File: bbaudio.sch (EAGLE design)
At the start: 38 parts, among them IC1 TLV320AIC3106, J1 AUDIO-JACKERTHENVAR, J2 AUDIO-JACKERTHENVAR, J3 AUDIO-JACKERTHENVAR, J4 AUDIO-JACKERTHENVAR, U2 V_REG_MIC2920, U3 LMZ14203, U4 VREG

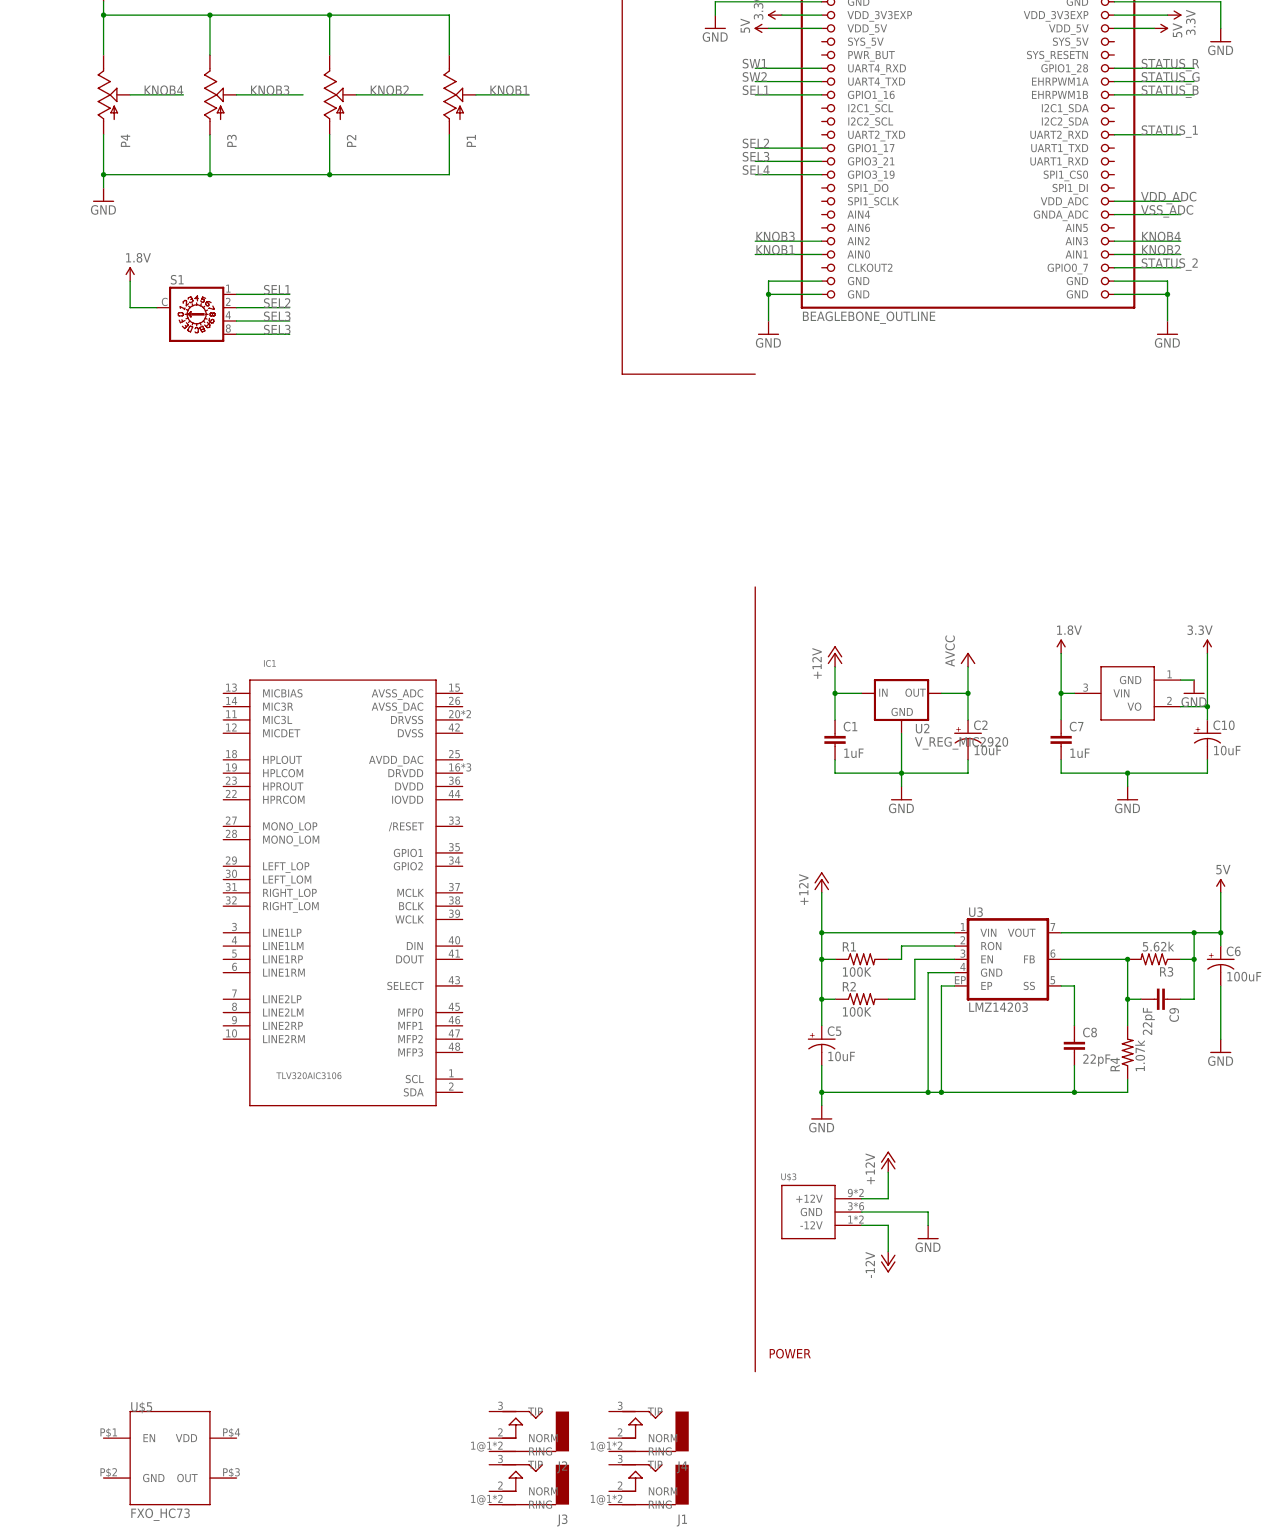
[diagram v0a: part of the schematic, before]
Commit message: Started wiring up the codec
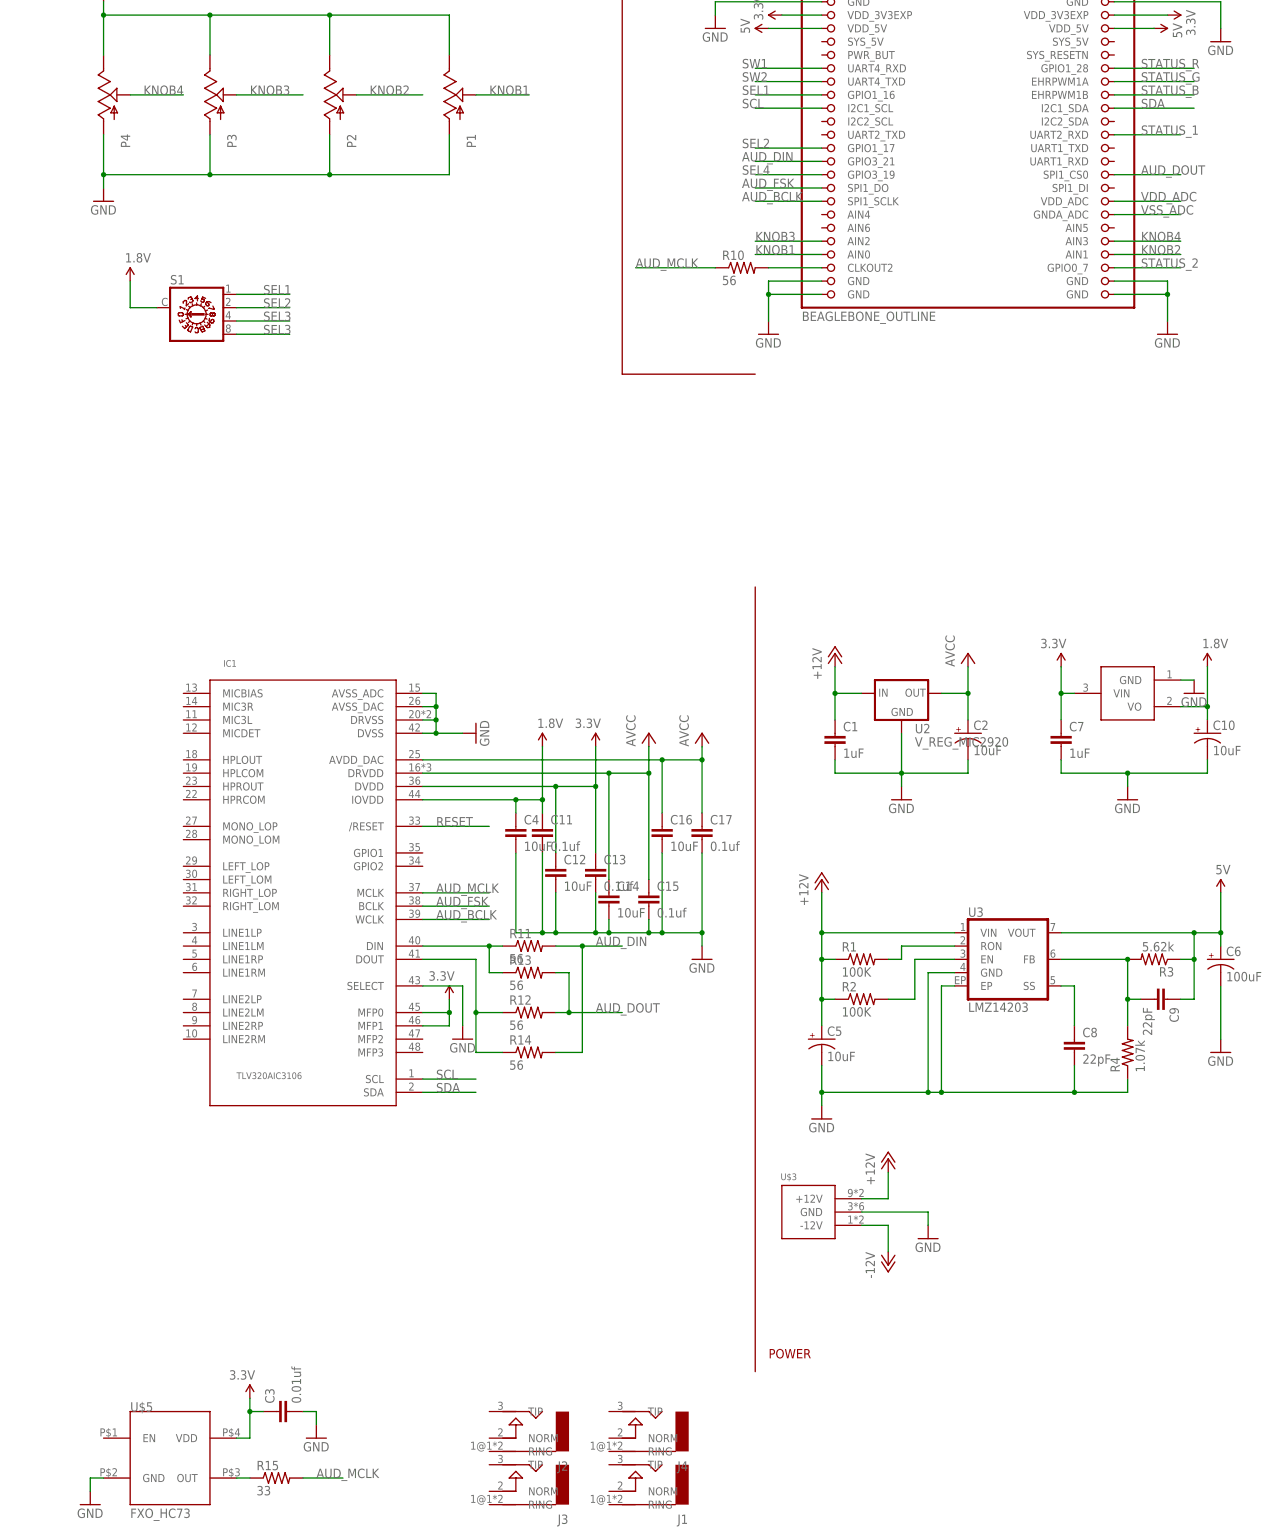
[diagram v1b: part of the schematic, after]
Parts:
- added C11, C13, C15, C17: 0.1uf, rcl:C-EUC0603
- added C12, C14, C16, C4: 10uF, rcl:C-EUC0603
- added C3: 0.01uf, rcl:C-EUC0603
- added R10, R11, R12, R13, R14: 56, SparkFun-Passives:RESISTOR0603-RES
- added R15: 33, SparkFun-Passives:RESISTOR0603-RES
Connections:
- new net AUD_BCLK: IC1.WCLK, U$1.SPI1_SCLK
- new net AUD_DIN: R11.2, R14.2, U$1.GPIO3_21
- new net AUD_DOUT: R12.2, R13.2, U$1.SPI1_CS0
- new net AUD_FSK: IC1.BCLK, U$1.SPI1_DO
- new net AUD_MCLK: IC1.MCLK, R10.1, R15.2
- new net N$10: IC1.DIN, R11.1, R13.1
- new net N$11: IC1.DOUT, R12.1, R14.1
- new net N$12: R15.1, U$5.OUT
- new net N$9: R10.2, U$1.CLKOUT2
- new net RESET: IC1./RESET
- new net SCL: IC1.SCL, U$1.I2C1_SCL
- new net SDA: IC1.SDA, U$1.I2C1_SDA
- net 1.8V: now also C10.+, C11.1, C4.1, IC1.IOVDD, U4.VO; no longer C7.1, U4.VIN
- net 3.3V: now also C12.1, C13.1, C3.1, C7.1, IC1.DVDD, IC1.MFP0, IC1.MFP1, U$5.VDD, U4.VIN; no longer C10.+, U4.VO
- net GND: now also C11.2, C12.2, C13.2, C14.2, C15.2, C16.2, C17.2, C3.2, C4.2, IC1.AVSS_ADC, IC1.AVSS_DAC, IC1.DRVSS, IC1.DVSS, IC1.SELECT, U$5.GND
- net SEL3: no longer U$1.GPIO3_21
- net VCC: now also C14.1, C15.1, C16.1, C17.1, IC1.AVDD_DAC, IC1.DRVDD
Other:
- moved on the sheet: IC1

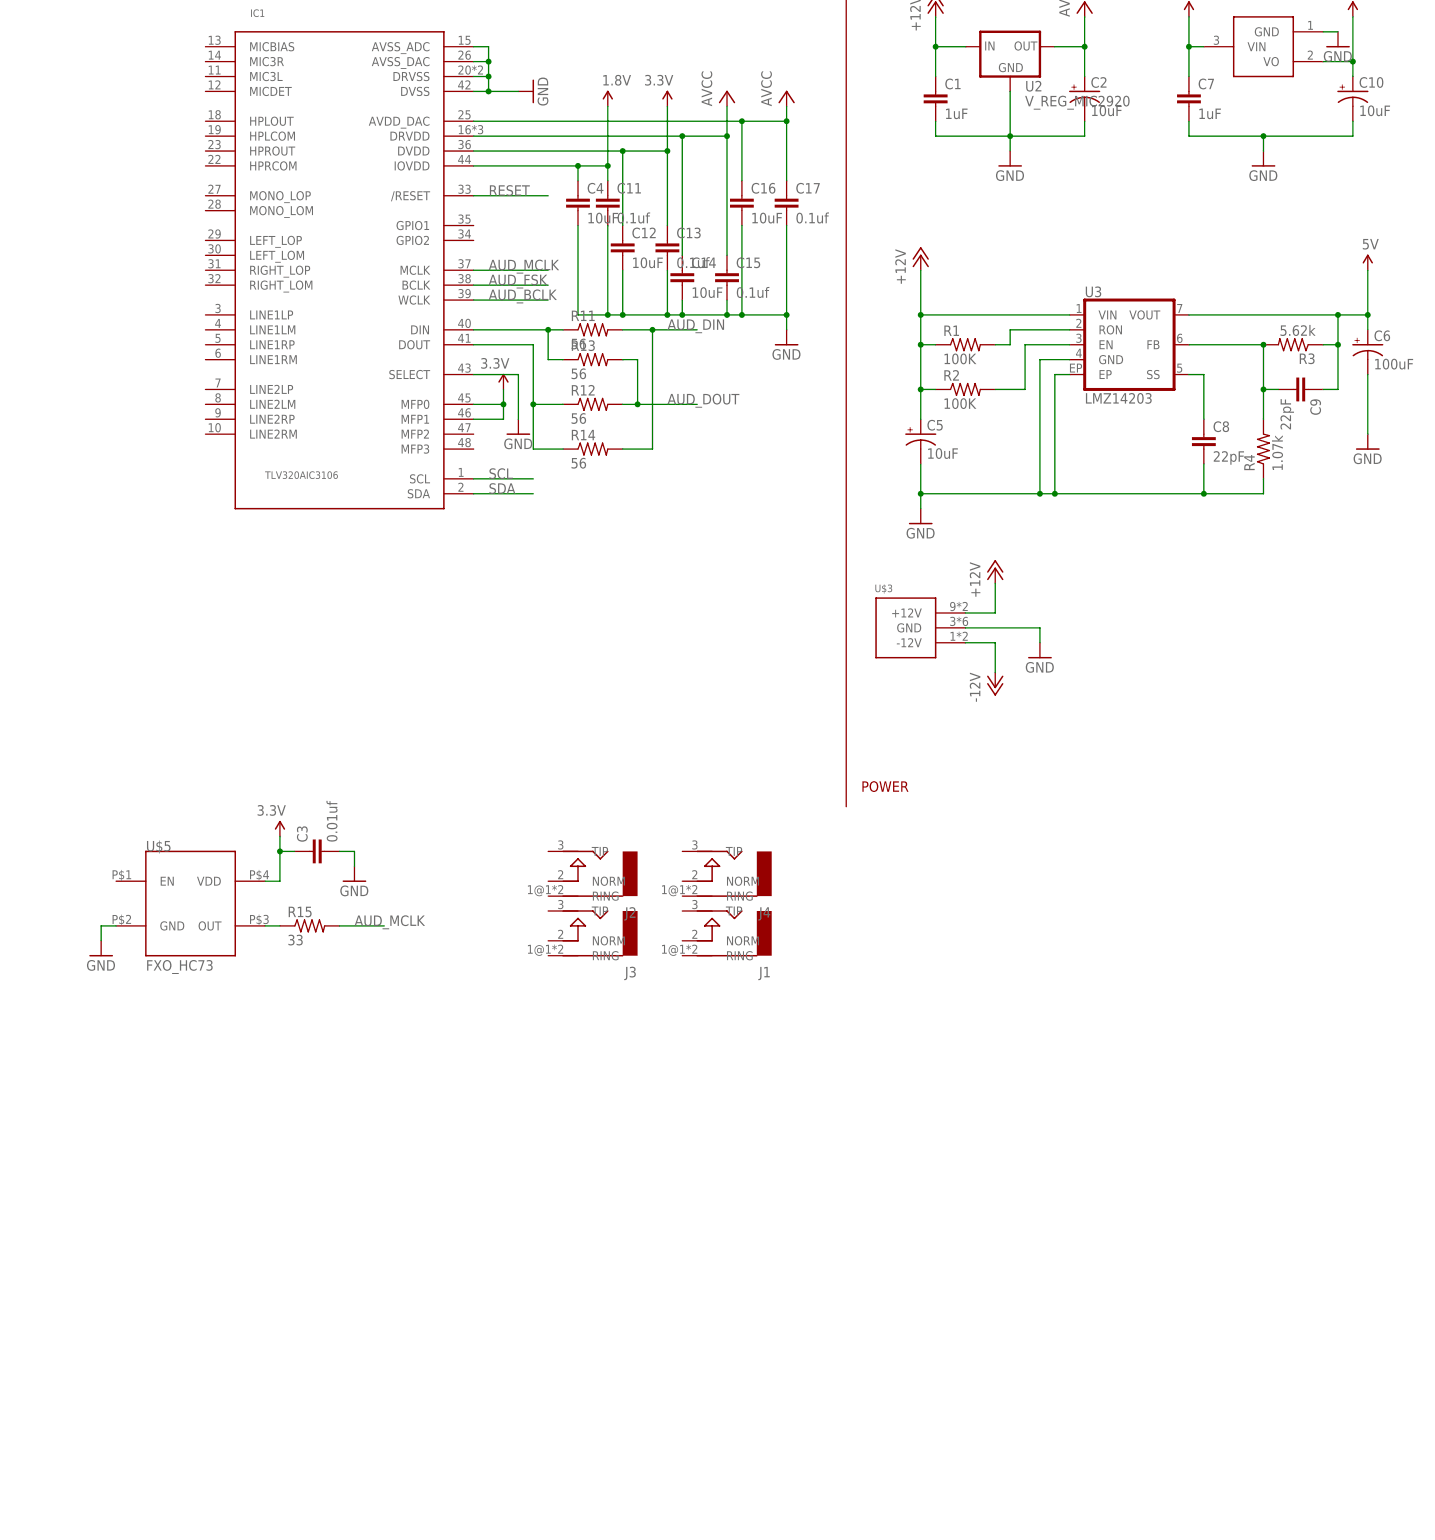
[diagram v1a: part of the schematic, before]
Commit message: Added audio i/o
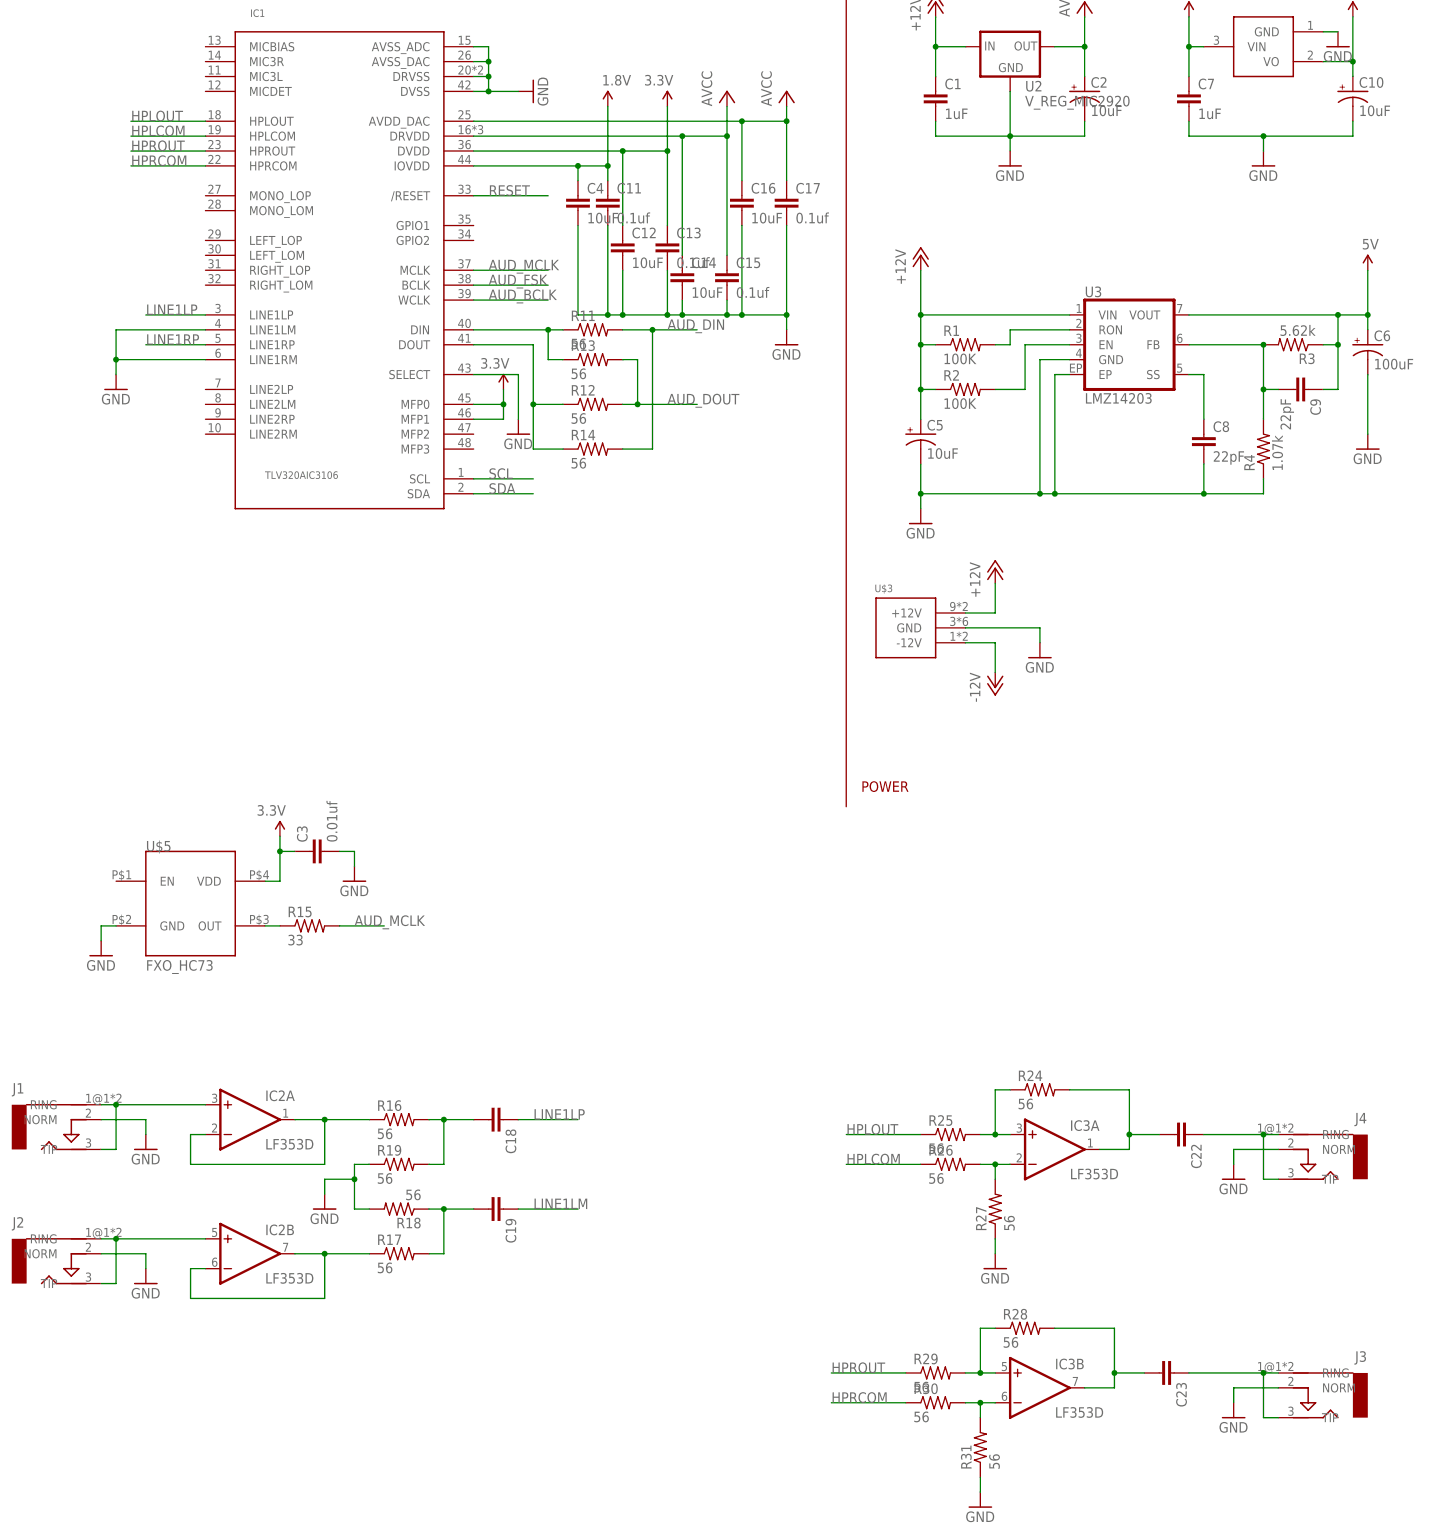
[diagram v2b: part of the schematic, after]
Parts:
- added C18, C19, C22, C23: (no value), SparkFun-Passives:CAP0805
- added IC2, IC3: LF353D, linear:LF353D
- added R16, R17, R18, R19, R24, R25, R26, R27, R28, R29, R30, R31: 56, SparkFun-Passives:RESISTOR0603-RES
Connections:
- new net HPLCOM: IC1.HPLCOM, R26.1
- new net HPLOUT: IC1.HPLOUT, R25.1
- new net HPRCOM: IC1.HPRCOM, R30.1
- new net HPROUT: IC1.HPROUT, R29.1
- new net LINE1LM: C19.1
- new net LINE1LP: C18.1, IC1.LINE1LP
- new net LINE1RP: IC1.LINE1RP
- new net N$14: IC2A.-IN, IC2A.OUT, R16.1
- new net N$15: C18.2, R16.2, R19.2
- new net N$16: IC2B.-IN, IC2B.OUT, R17.1
- new net N$17: C19.2, R17.2, R18.1
- new net N$18: IC2A.+IN, J1.RING, J1.TIP
- new net N$19: IC2B.+IN, J2.RING, J2.TIP
- new net N$20: C22.1, J4.RING, J4.TIP
- new net N$27: C22.2, IC3A.OUT, R24.2
- new net N$28: IC3A.+IN, R24.1, R25.2
- new net N$29: IC3A.-IN, R26.2, R27.2
- new net N$31: C23.2, IC3B.OUT, R28.2
- new net N$32: IC3B.+IN, R28.1, R29.2
- new net N$33: IC3B.-IN, R30.2, R31.2
- new net N$34: C23.1, J3.RING, J3.TIP
- net GND: now also IC1.LINE1LM, IC1.LINE1RM, J1.NORM, J2.NORM, J3.NORM, J4.NORM, R18.2, R19.1, R27.1, R31.1
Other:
- moved on the sheet: J1, J2, J3, J4

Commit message: Re-did the audio I/O stuff
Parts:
- removed C18, C22, C23: (no value), SparkFun-Passives:CAP0805
- removed R16: 56, SparkFun-Passives:RESISTOR0603-RES
- added 10K, R22: 20k, SparkFun-Passives:RESISTOR0603-RES
- added IC4: LF353D, linear:LF353D
- added R20, R21, R23, R33: 100K, SparkFun-Passives:RESISTOR0603-RES
- added R32: 100k, SparkFun-Passives:RESISTOR0603-RES
- added R34, R35: 1K, SparkFun-Passives:RESISTOR0603-RES
- C19: value (none) -> 0.1uF; device SparkFun-Passives:CAP0805 -> rcl:C-EUC0603
- R17, R19, R24, R27, R28, R29, R30, R31: value 56 -> 100K
- R18: value 56 -> 100k
- R25, R26: value 56 -> 71K
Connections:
- removed net LINE1LM: C19.1
- removed net N$16: IC2B.-IN, IC2B.OUT, R17.1
- new net AUD_REF: IC1.LINE1LM, IC1.LINE1RM, IC2B.+IN, IC4B.+IN, R20.1, R21.2
- new net MICBIAS: C19.1, IC1.MICBIAS, R20.2
- new net N$21: IC4A.-IN, R22.1, R23.2
- new net N$22: IC4A.OUT, R22.2, R33.1
- new net N$23: IC4B.-IN, R32.1, R33.2
- net GND: now also C19.2, IC2A.+IN, IC4A.+IN, R21.1; no longer IC1.LINE1LM, IC1.LINE1RM, R18.2, R19.1
- net LINE1LP: now also IC2B.OUT, R18.2; no longer C18.1
- net LINE1RP: now also IC4B.OUT, R32.2
- net N$14: now also 10K.2, R19.1; no longer IC2A.-IN, R16.1
- net N$15: now also IC2B.-IN, R18.1; no longer C18.2, R16.2
- net N$17: now also 10K.1, IC2A.-IN; no longer C19.2, R18.1
- net N$18: now also R17.1; no longer IC2A.+IN
- net N$19: now also R23.1; no longer IC2B.+IN
- net N$20: now also R34.2; no longer C22.1
- net N$27: now also R34.1; no longer C22.2
- net N$31: now also R35.1; no longer C23.2
- net N$34: now also R35.2; no longer C23.1
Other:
- moved on the sheet: C19, IC2A, IC2B, J1, J2, R17, R18, R19, R25, R29
